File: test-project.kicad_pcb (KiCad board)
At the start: 2 copper layers, 116.8 x 64.8 mm, 21 parts, among them P1 CONN_01X06, P2 CONN_01X02, U1 74HC14, U2 OP275

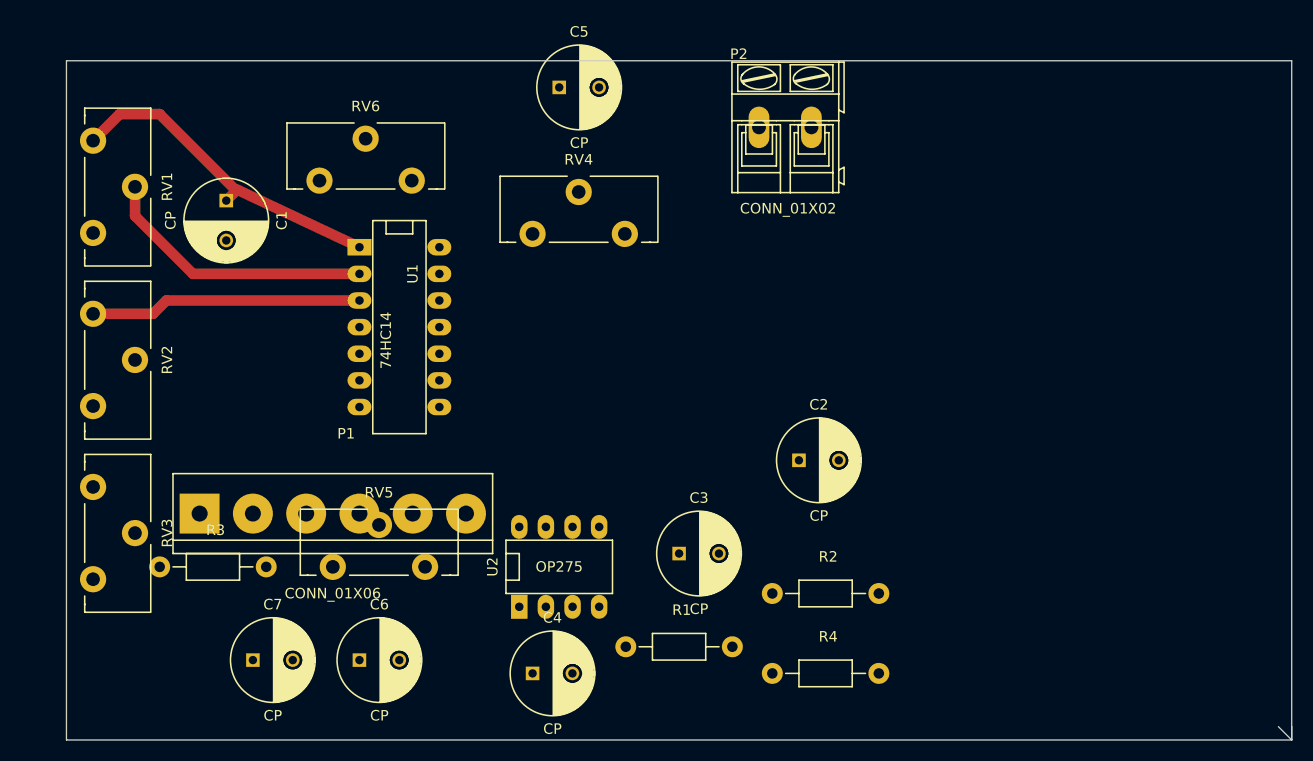
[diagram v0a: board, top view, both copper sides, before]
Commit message: first try for the pcb counter is missing some files need to be deleted from the repo
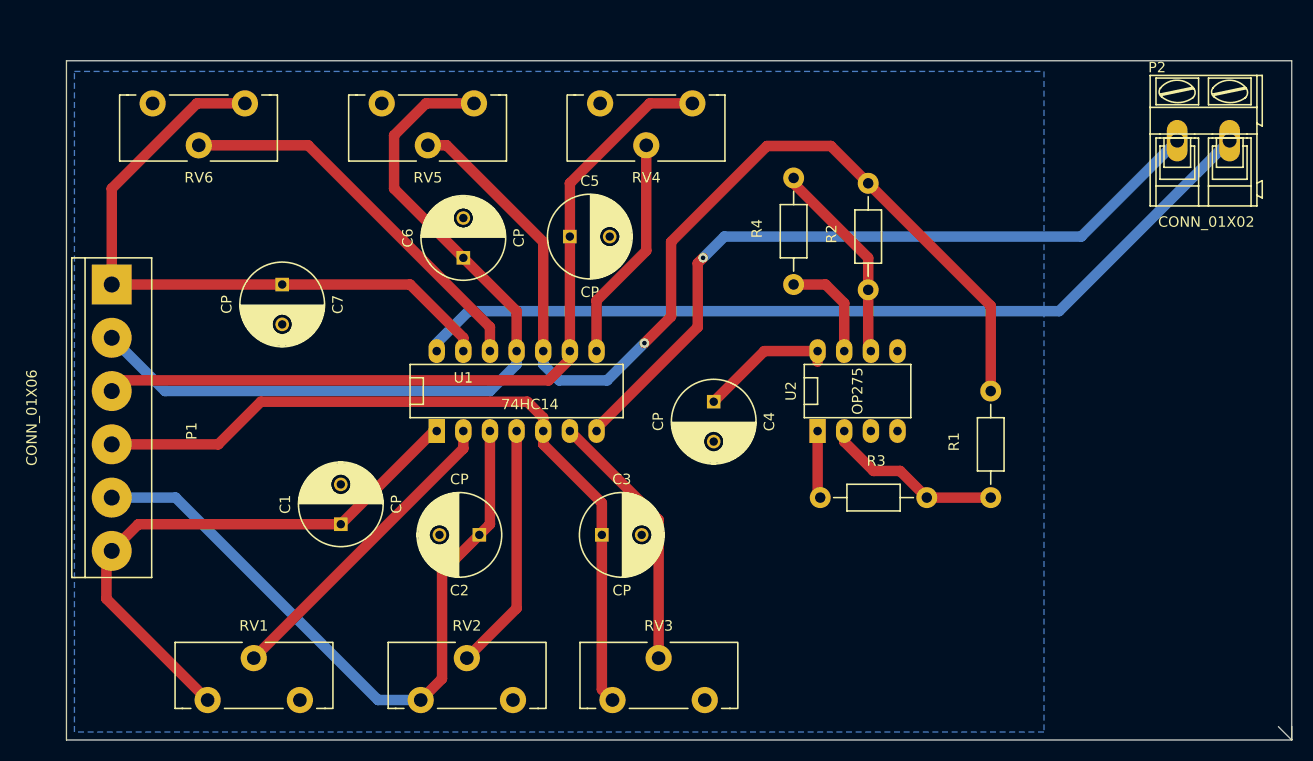
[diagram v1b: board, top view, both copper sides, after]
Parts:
- moved R3 63.3 mm to (220.5, 138.2)
- moved RV1 54.4 mm to (157.0, 157.5), turned to 0 degrees
- moved RV3 53.5 mm to (195.6, 157.5), turned to 0 degrees
- moved RV2 48.3 mm to (177.3, 157.5), turned to 0 degrees
- moved RV5 46.2 mm to (182.4, 100.6), turned to 180 degrees
- moved R4 42.3 mm to (212.9, 112.8), turned to 90 degrees
- moved P2 39.9 mm to (249.4, 104.1)
- moved C6 39.6 mm to (181.4, 115.3), turned to 90 degrees
- moved C7 35.9 mm to (164.1, 117.9), turned to 270 degrees
- moved R1 35.4 mm to (231.6, 133.1), turned to 90 degrees
- moved R2 34.3 mm to (220.0, 113.3), turned to 90 degrees
- moved U2 33.0 mm to (218.9, 128.0)
- moved C1 32.7 mm to (169.7, 140.7), turned to 90 degrees
- moved C2 31.3 mm to (182.9, 141.7), turned to 180 degrees
- moved C4 31.1 mm to (205.2, 129.0), turned to 270 degrees
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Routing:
- net Net-(R1-Pad2): track 0.00 -> 97.7 mm, vias 0 -> 1
- net Net-(P2-Pad2): track 0.00 -> 84.4 mm
- net Net-(C6-Pad1): track 0.00 -> 77.3 mm
- net Net-(C5-Pad1): track 0.00 -> 76.6 mm
- net Net-(C3-Pad1): track 0.00 -> 73.1 mm
- net Net-(P2-Pad1): track 0.00 -> 70.6 mm, vias 0 -> 1
- net Net-(C7-Pad1): track 0.00 -> 62.1 mm
- net Net-(C2-Pad1): track 25.9 -> 65.8 mm
- net Net-(RV6-Pad2): track 0.00 -> 37.2 mm
- net Net-(RV3-Pad2): track 0.00 -> 25.2 mm
- net Net-(RV2-Pad2): track 0.00 -> 23.6 mm
- net Net-(C1-Pad1): track 32.1 -> 54.2 mm
- net Net-(RV4-Pad2): track 0.00 -> 21.6 mm
- net Net-(R2-Pad1): track 0.00 -> 19.9 mm
- net Net-(R1-Pad1): track 0.00 -> 17.2 mm
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- added copper zone on B.Cu, net GND

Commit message: updated some of the connections
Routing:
- net Net-(RV3-Pad2): track 25.2 -> 28.1 mm
- net Net-(C3-Pad1): track 73.1 -> 74.4 mm
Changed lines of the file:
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@@
     (thickness 1.6)
     (drawings 6)
-    (tracks 107)
+    (tracks 110)
     (zones 0)
     (modules 21)
@@
   (segment (start 183.896 131.826) (end 183.896 140.716) (width 1) (layer F.Cu) (net 3))
   (segment (start 183.896 140.716) (end 182.88 141.732) (width 1) (layer F.Cu) (net 3))
-  (segment (start 188.976 131.826) (end 188.976 130.556) (width 1) (layer F.Cu) (net 4))
-  (segment (start 157.988 133.096) (end 147.828 133.096) (width 1) (layer F.Cu) (net 4))
-  (segment (start 162.052 129.032) (end 157.988 133.096) (width 1) (layer F.Cu) (net 4))
-  (segment (start 187.452 129.032) (end 162.052 129.032) (width 1) (layer F.Cu) (net 4))
-  (segment (start 188.976 130.556) (end 187.452 129.032) (width 1) (layer F.Cu) (net 4))
-  (segment (start 188.976 131.826) (end 188.976 133.096) (width 1) (layer F.Cu) (net 4))
-  (segment (start 194.564 138.684) (end 194.564 141.732) (width 1) (layer F.Cu) (net 4))
-  (segment (start 188.976 133.096) (end 194.564 138.684) (width 1) (layer F.Cu) (net 4))
+  (segment (start 188.976 131.826) (end 188.976 129.032) (width 1) (layer F.Cu) (net 4) (status 400000))
+  (segment (start 164.084 133.096) (end 147.828 133.096) (width 1) (layer F.Cu) (net 4) (status 800000))
+  (segment (start 168.656 128.524) (end 164.084 133.096) (width 1) (layer F.Cu) (net 4))
+  (segment (start 188.468 128.524) (end 168.656 128.524) (width 1) (layer F.Cu) (net 4))
+  (segment (start 188.976 129.032) (end 188.468 128.524) (width 1) (layer F.Cu) (net 4))
+  (segment (start 188.976 131.826) (end 188.976 136.144) (width 1) (layer F.Cu) (net 4) (status 400000))
+  (segment (start 188.976 136.144) (end 194.564 141.732) (width 1) (layer F.Cu) (net 4) (status 800000))
   (segment (start 194.564 141.732) (end 194.564 156.464) (width 1) (layer F.Cu) (net 4) (status 10))
   (segment (start 194.564 156.464) (end 195.58 157.48) (width 1) (layer F.Cu) (net 4))
@@
   (segment (start 186.436 131.826) (end 186.436 148.73732) (width 1) (layer F.Cu) (net 17))
   (segment (start 186.436 148.73732) (end 181.69128 153.48204) (width 1) (layer F.Cu) (net 17))
-  (segment (start 199.97928 153.48204) (end 199.97928 140.28928) (width 1) (layer F.Cu) (net 18))
-  (segment (start 199.97928 140.28928) (end 191.516 131.826) (width 1) (layer F.Cu) (net 18))
+  (segment (start 191.516 131.826) (end 191.516 136.144) (width 1) (layer F.Cu) (net 18) (status 400000))
+  (segment (start 200.66 141.224) (end 200.66 152.80132) (width 1) (layer F.Cu) (net 18) (status 800000))
+  (segment (start 198.628 139.192) (end 200.66 141.224) (width 1) (layer F.Cu) (net 18))
+  (segment (start 194.564 139.192) (end 198.628 139.192) (width 1) (layer F.Cu) (net 18))
+  (segment (start 191.516 136.144) (end 194.564 139.192) (width 1) (layer F.Cu) (net 18))
+  (segment (start 200.66 152.80132) (end 199.97928 153.48204) (width 1) (layer F.Cu) (net 18) (status C00000))
   (segment (start 194.056 124.206) (end 194.056 119.38) (width 1) (layer F.Cu) (net 19))
   (segment (start 198.80072 114.63528) (end 198.80072 104.58196) (width 1) (layer F.Cu) (net 19))
